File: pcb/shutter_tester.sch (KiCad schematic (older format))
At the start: 20 parts

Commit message: first draft pcb
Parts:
- removed D? (x3): LED, symbol Device:LED
- removed J? (x4): BNC, symbol Connector:Conn_Coaxial
- removed Q? (x8): 2N2222a, symbol Device:Q_NPN_CBE
- removed R? (x3): 2k2, symbol Device:R
- added BT1: 2x AA, Connector_PinHeader_2.54mm:PinHeader_1x02_P2.54mm_Horizontal, symbol Device:Battery
- added D1, D2, D4: LED, LED_THT:LED_D3.0mm, symbol Device:LED
- added H1, H2, H3, H4: MountingHole, MountingHole:MountingHole_3.2mm_M3, symbol Mechanical:MountingHole
- added J1, J2, J3, J4: Conn_01x02, Connector_PinHeader_2.54mm:PinHeader_1x02_P2.54mm_Horizontal, symbol Connector_Generic:Conn_01x02
- added JP1, JP2, JP3: 0R, Resistor_SMD:R_1206_3216Metric, symbol Device:Jumper_NC_Small
- added Q1, Q2, Q3, Q4: MMBTA13LT3G, Package_TO_SOT_SMD:SOT-23, symbol Device:Q_NPN_Darlington_BEC
- added R1, R2, R4: 2k, Resistor_SMD:R_0805_2012Metric_Pad1.20x1.40mm_HandSolder, symbol Device:R
- D3: renamed from D?; footprint (none) -> LED_THT:LED_D3.0mm
- R3: renamed from R?; value 2k2 -> 2k; footprint (none) -> Resistor_SMD:R_0805_2012Metric_Pad1.20x1.40mm_HandSolder
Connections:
- net GND: now also BT1.2 (-), J1.2 (Pin_2), J2.2 (Pin_2), J3.2 (Pin_2), J4.2 (Pin_2), Q1.2 (E), Q2.2 (E), Q3.2 (E), Q4.2 (E)
- net VCC: now also BT1.1 (+), D1.1 (K), D2.1 (K), D4.1 (K), R1.1, R2.1, R4.1
- net at D3.2 (A): now also Q3.1 (B)
- net at R3.2: now also J3.1 (Pin_1), Q3.3 (C)
- new net: D1.2 (A), JP1.2
- new net: J1.1 (Pin_1), Q1.3 (C), R1.2
- new net: JP1.1, Q1.1 (B)
- new net: D4.2 (A), JP3.2
- new net: J4.1 (Pin_1), Q4.3 (C), R4.2
- new net: JP3.1, Q4.1 (B)
- new net: D2.2 (A), JP2.2
- new net: J2.1 (Pin_1), Q2.3 (C), R2.2
- new net: JP2.1, Q2.1 (B)
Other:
- moved on the sheet: D3, R3

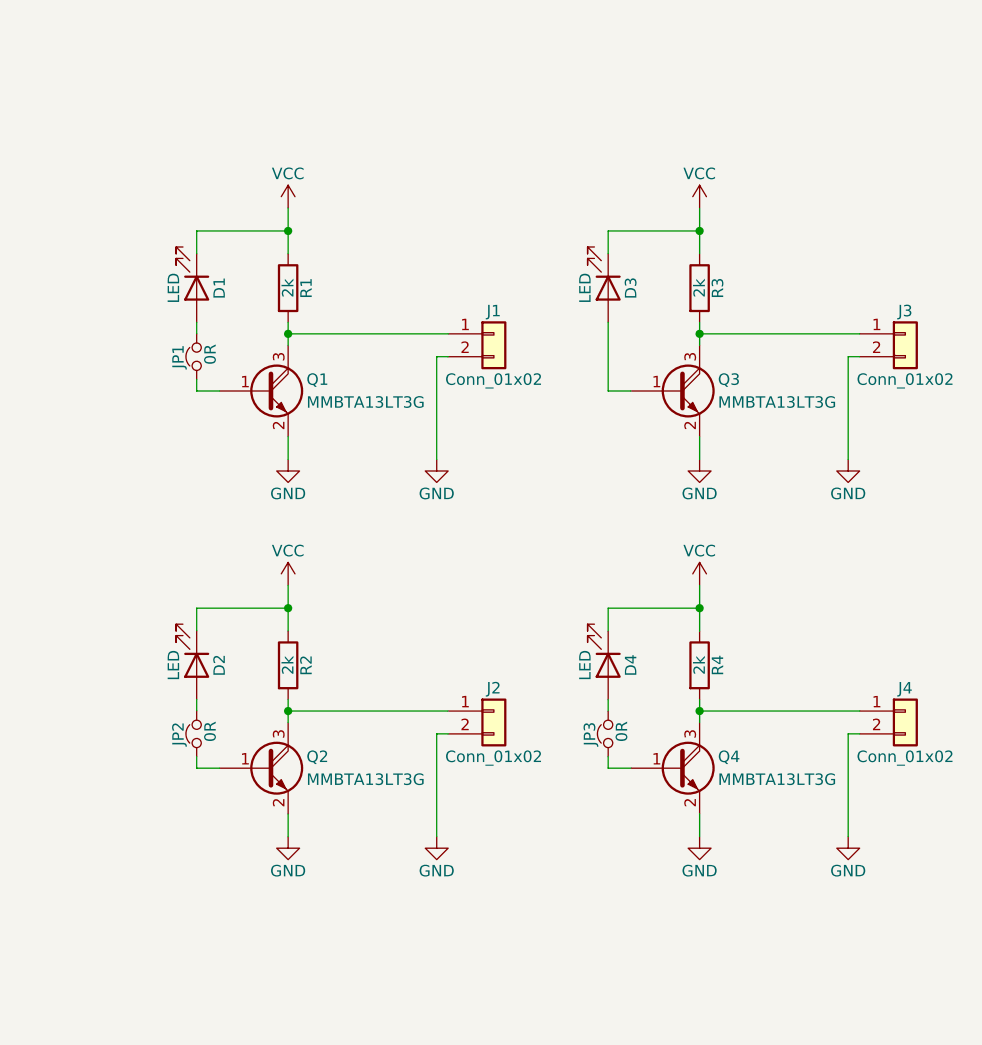
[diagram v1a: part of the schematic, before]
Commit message: change to single light sensor
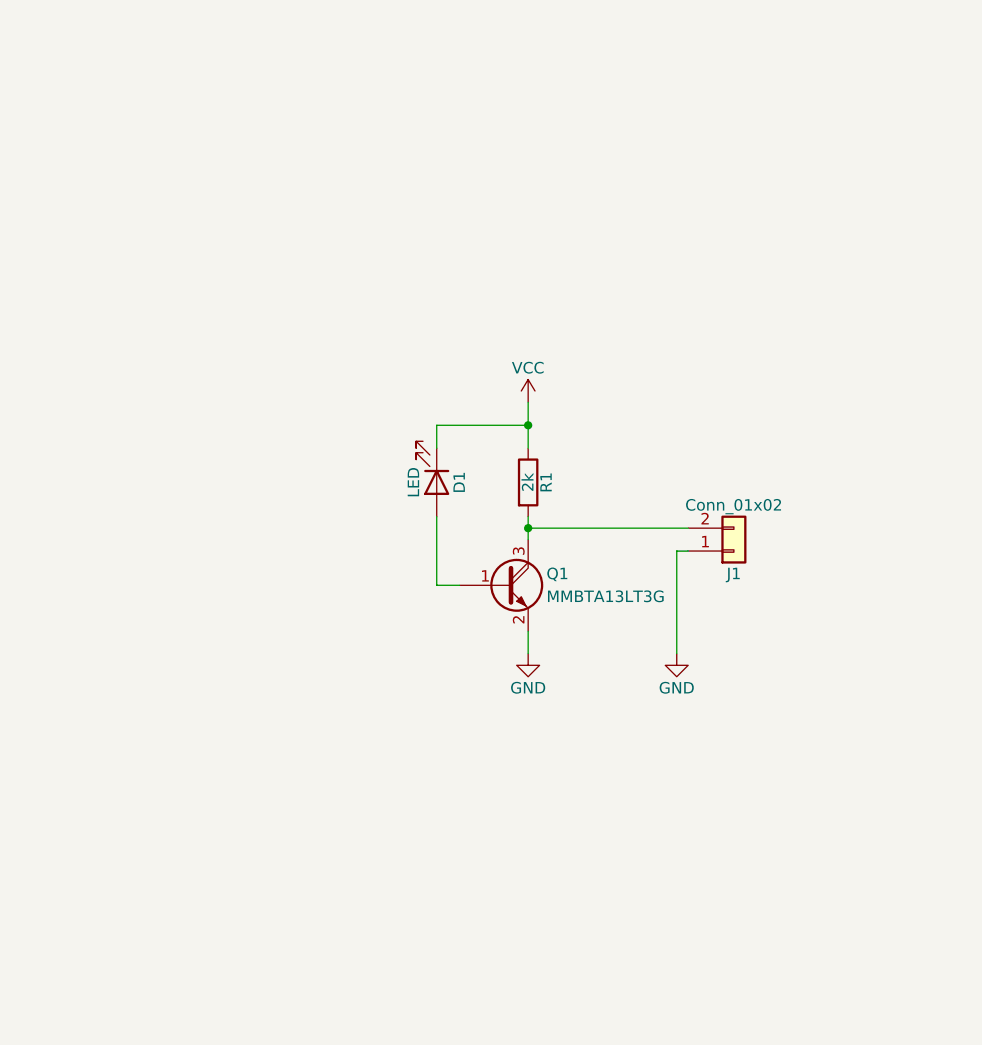
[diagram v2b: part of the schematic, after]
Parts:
- removed D2, D3, D4: LED, LED_THT:LED_D3.0mm, symbol Device:LED
- removed J2, J3, J4: Conn_01x02, Connector_PinHeader_2.54mm:PinHeader_1x02_P2.54mm_Horizontal, symbol Connector_Generic:Conn_01x02
- removed JP1, JP2, JP3: 0R, Resistor_SMD:R_1206_3216Metric, symbol Device:Jumper_NC_Small
- removed Q2, Q3, Q4: MMBTA13LT3G, Package_TO_SOT_SMD:SOT-23, symbol Device:Q_NPN_Darlington_BEC
- removed R2, R3, R4: 2k, Resistor_SMD:R_0805_2012Metric_Pad1.20x1.40mm_HandSolder, symbol Device:R
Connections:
- net GND: now also J1.1 (Pin_1); no longer J1.2 (Pin_2)
- net at D1.2 (A): now also Q1.1 (B)
- net at Q1.3 (C), R1.2: now also J1.2 (Pin_2); no longer J1.1 (Pin_1)
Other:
- moved on the sheet: D1, J1, Q1, R1

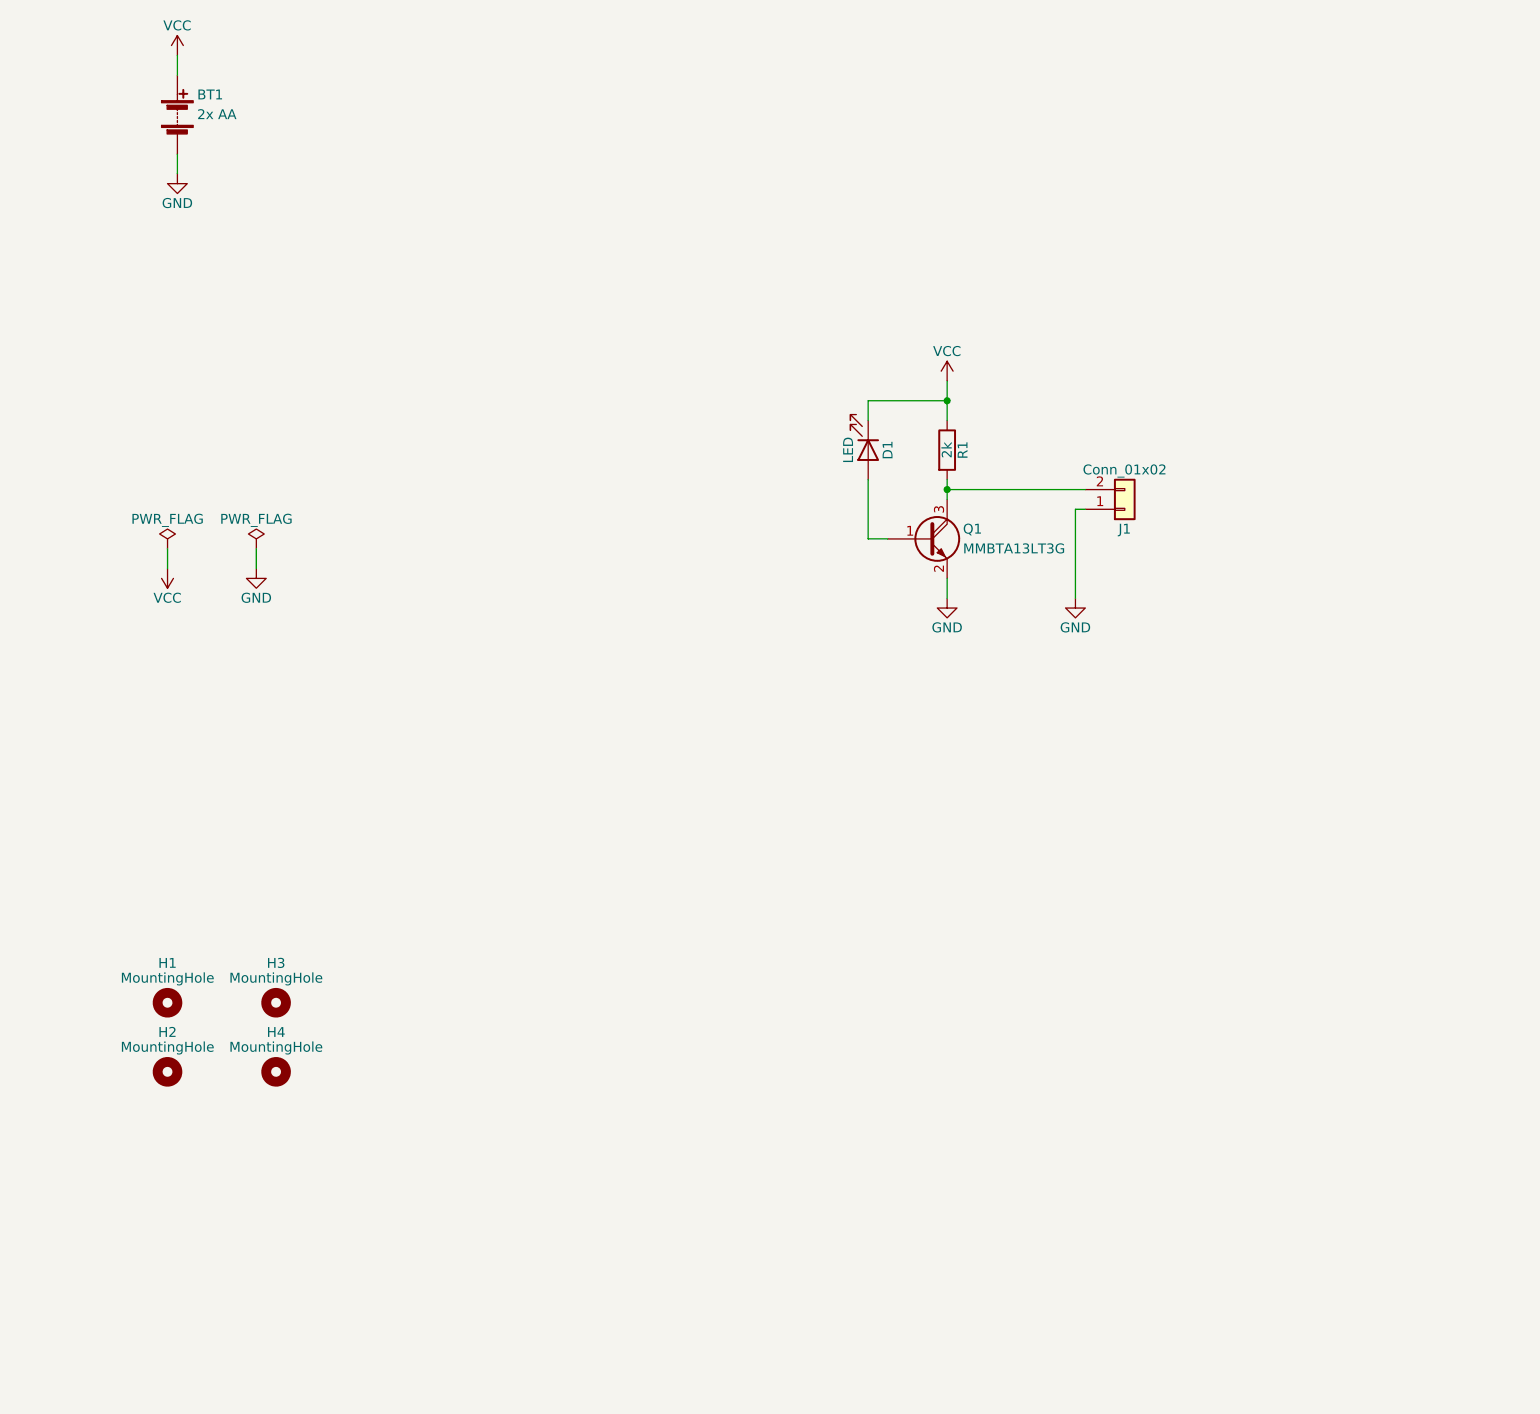
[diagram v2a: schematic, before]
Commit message: add comparator circuit
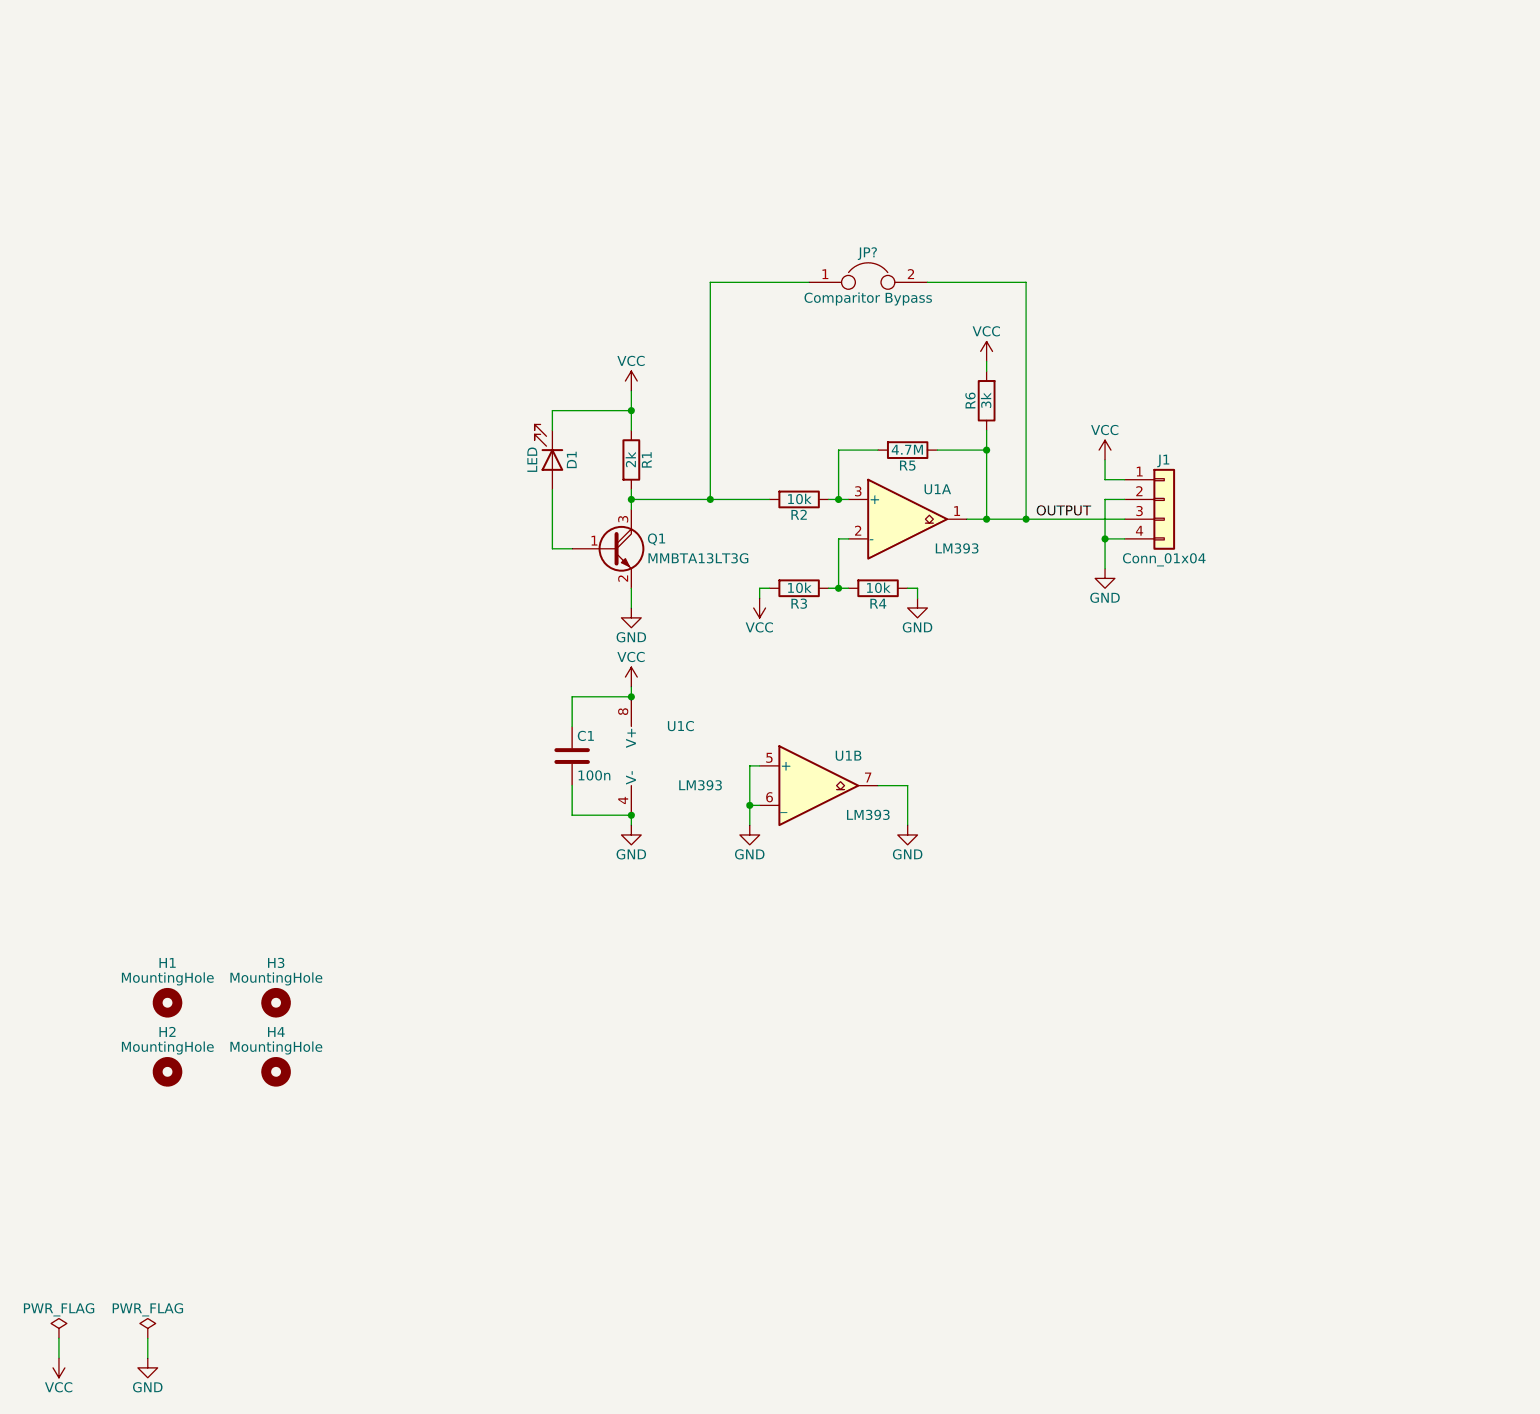
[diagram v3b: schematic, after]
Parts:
- removed BT1: 2x AA, Connector_PinHeader_2.54mm:PinHeader_1x02_P2.54mm_Horizontal, symbol Device:Battery
- removed J1: Conn_01x02, Connector_PinHeader_2.54mm:PinHeader_1x02_P2.54mm_Horizontal, symbol Connector_Generic:Conn_01x02
- added C1: 100n, Capacitor_SMD:C_0805_2012Metric_Pad1.18x1.45mm_HandSolder, symbol Device:C
- added J1: Conn_01x04, Connector_PinHeader_2.54mm:PinHeader_1x04_P2.54mm_Horizontal, symbol Connector_Generic:Conn_01x04
- added JP?: Comparitor Bypass, Resistor_SMD:R_1206_3216Metric_Pad1.30x1.75mm_HandSolder, symbol Device:Jumper
- added R2, R3, R4: 10k, Resistor_SMD:R_1206_3216Metric_Pad1.30x1.75mm_HandSolder, symbol Device:R
- added R5: 4.7M, Resistor_SMD:R_0603_1608Metric_Pad0.98x0.95mm_HandSolder, symbol Device:R
- added R6: 3k, Resistor_SMD:R_0805_2012Metric_Pad1.20x1.40mm_HandSolder, symbol Device:R
- added U1: LM393, Package_SO:SOP-8_3.9x4.9mm_P1.27mm, symbol Comparator:LM393
- D1: footprint LED_THT:LED_D3.0mm -> LED_SMD:LED_0603_1608Metric_Pad1.05x0.95mm_HandSolder
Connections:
- net GND: now also C1.2, J1.2 (Pin_2), J1.4 (Pin_4), R4.1, U1.4 (V-), U1.5 (+), U1.6 (_), U1.7
- net VCC: now also C1.1, J1.1 (Pin_1), R3.2, R6.2, U1.8 (V+)
- net at Q1.3 (C), R1.2: now also JP?.1, R2.2
- new net: R3.1, R4.2, U1.2 (-)
- new net: R2.1, R5.2, U1.3 (+)
- new net OUTPUT: J1.3 (Pin_3), JP?.2, R5.1, R6.1, U1.1
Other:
- moved on the sheet: D1, Q1, R1
